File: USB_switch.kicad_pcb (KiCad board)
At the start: 2 copper layers, 29 x 44 mm, 16 parts, among them J1 USB_A, Q1 Q_PMOS_GSD, SW1 SW_SPDT

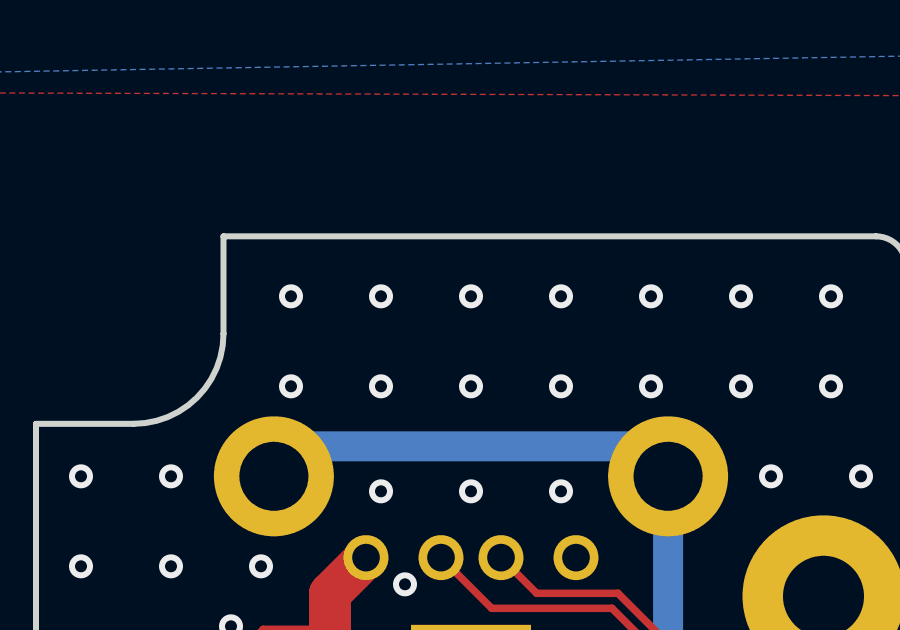
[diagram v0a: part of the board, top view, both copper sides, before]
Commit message: Added Rev on silkscreen.
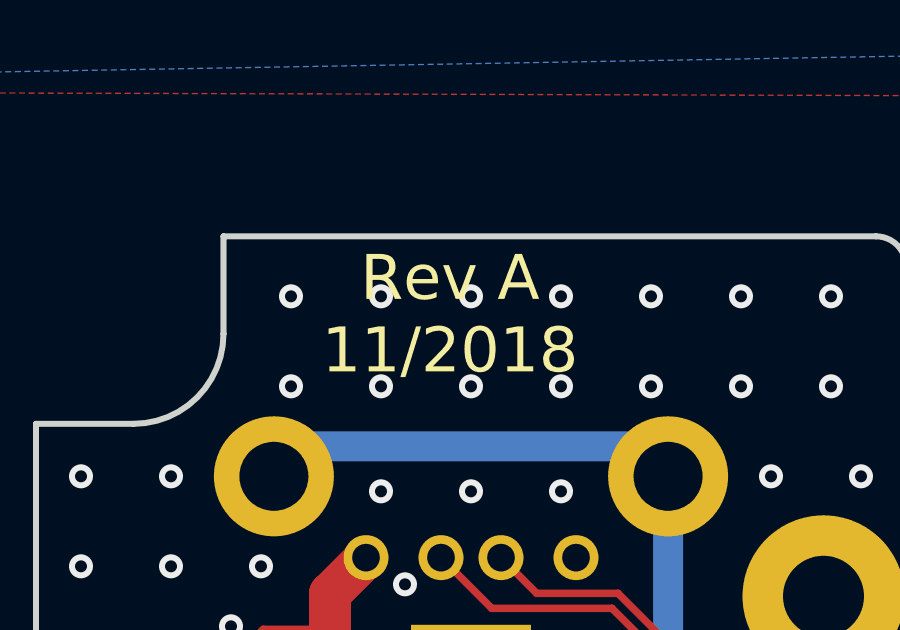
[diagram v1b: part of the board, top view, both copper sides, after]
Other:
- board text added: "Rev A 11/2018"
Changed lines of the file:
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@@
   (general
     (thickness 1.6)
-    (drawings 20)
+    (drawings 21)
     (tracks 113)
     (zones 0)
@@
       (rotate (xyz 0 0 0))
     )
+  )
+  (gr_text "Rev A\n11/2018" (at 99.3 80.6) (layer F.SilkS)
+    (effects (font (size 1.5 1.5) (thickness 0.3)))
   )
   (gr_circle (center 103 114.5) (end 104.5 114.5) (layer Edge.Cuts) (width 0.15))
@@
     (connect_pads (clearance 0.2))
     (min_thickness 0.18)
-    (fill yes (arc_segments 16) (thermal_gap 0.2) (thermal_bridge_width 0.508))
+    (fill yes (arc_segments 32) (thermal_gap 0.2) (thermal_bridge_width 0.508))
     (polygon
       (pts
@@
     (connect_pads (clearance 0.2))
     (min_thickness 0.18)
-    (fill yes (arc_segments 16) (thermal_gap 0.2) (thermal_bridge_width 0.508))
+    (fill yes (arc_segments 32) (thermal_gap 0.2) (thermal_bridge_width 0.508))
     (polygon
       (pts
